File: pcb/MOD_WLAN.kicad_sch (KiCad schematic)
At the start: 21 parts, among them IC2 ESP32-C6-WROOM-1-N8, SW1 SW_DIP_x01

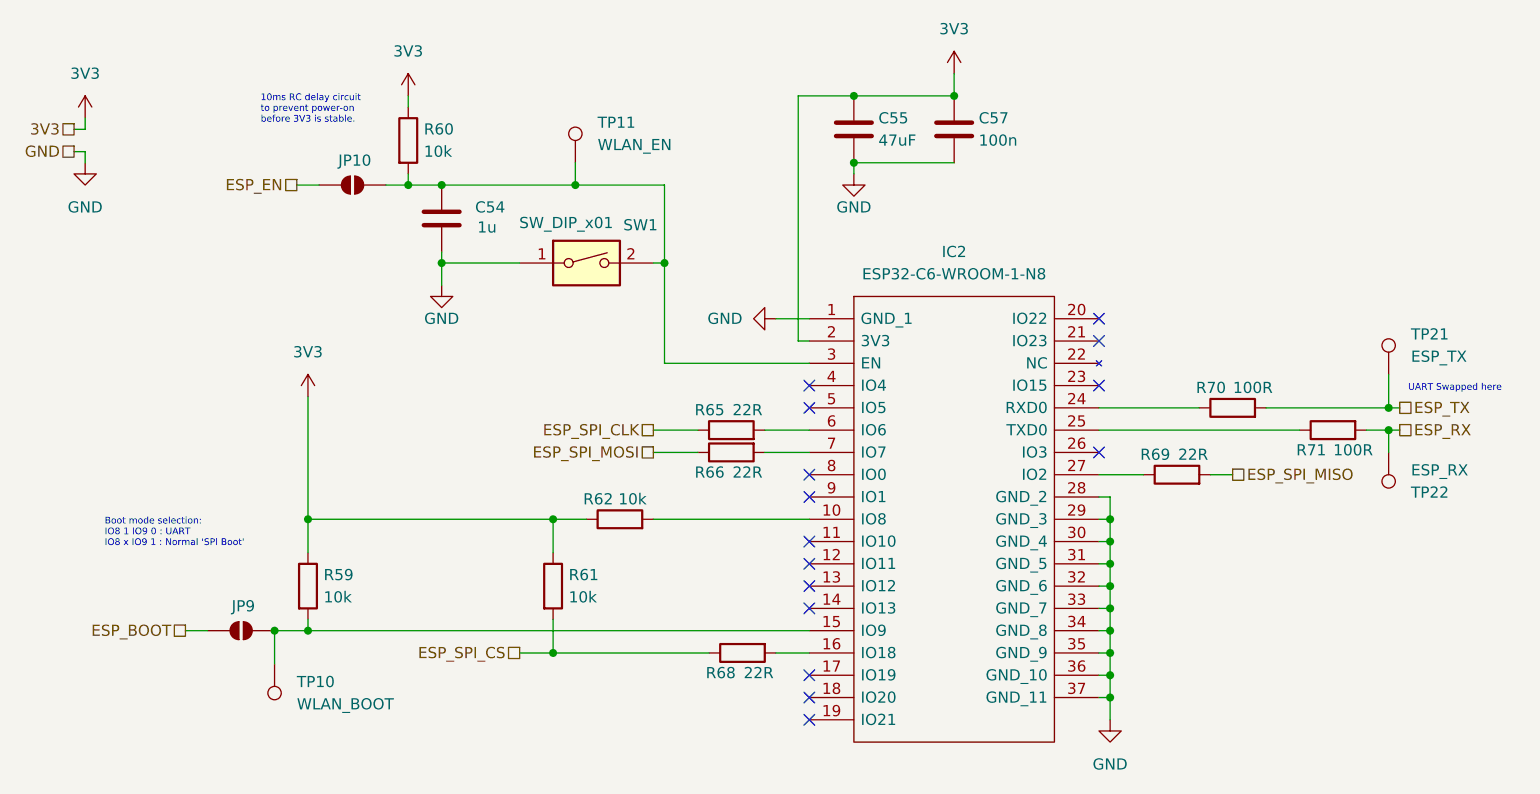
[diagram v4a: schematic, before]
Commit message: initial routing of power for pcie, swapped switches for jumpers
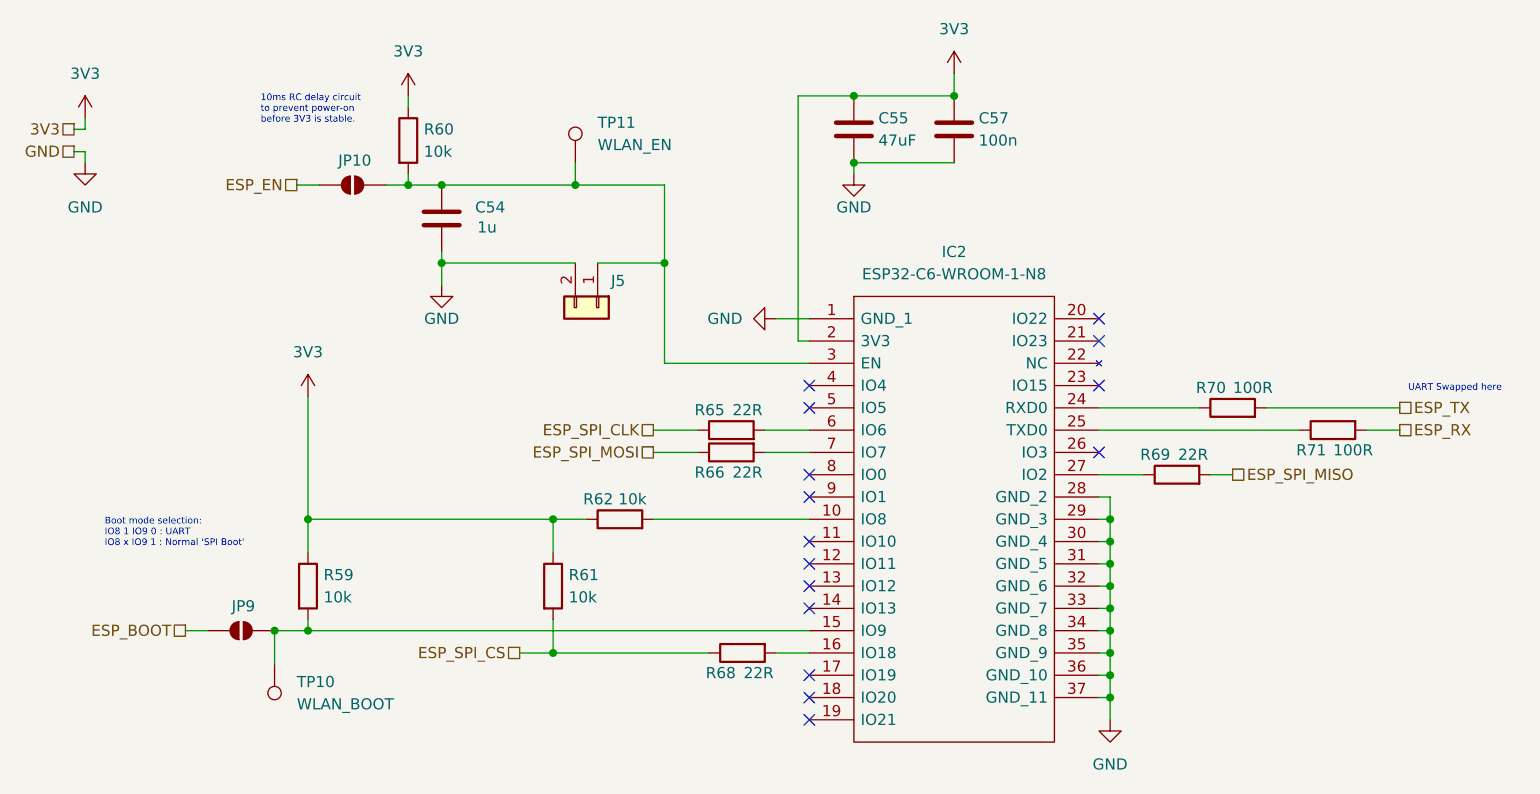
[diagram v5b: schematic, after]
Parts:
- removed SW1: SW_DIP_x01, SamacSys_Parts:EDS01SGNNTR04Q, symbol Switch:SW_DIP_x01
- removed TP21: ESP_TX, TestPoint:TestPoint_THTPad_D2.0mm_Drill1.0mm, symbol Connector:TestPoint
- removed TP22: ESP_RX, TestPoint:TestPoint_THTPad_D2.0mm_Drill1.0mm, symbol Connector:TestPoint
- added J5: Conn_01x02, Connector_PinHeader_2.54mm:PinHeader_1x02_P2.54mm_Vertical, symbol Connector_Generic:Conn_01x02
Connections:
- net GND: now also J5.2 (Pin_2)
- net at C54.1, IC2.3 (EN), JP10.2 (B)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: now also J5.1 (Pin_1)
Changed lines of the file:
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@@
-	)
-	(junction
-		(at 175.26 57.15)
-		(diameter 0)
-		(color 0 0 0 0)
 	)
 	(junction
@@
 	)
 	(junction
-		(at 175.26 59.69)
-		(diameter 0)
-		(color 0 0 0 0)
-	)
-	(junction
 		(at 143.51 87.63)
 		(diameter 0)
@@
 	(wire
 		(pts
-			(xy 67.31 40.64) (xy 76.2 40.64)
+			(xy 67.31 40.64) (xy 82.55 40.64)
 		)
 		(stroke
@@
 	(wire
 		(pts
-			(xy 92.71 40.64) (xy 91.44 40.64)
-		)
-		(stroke
-			(width 0)
-			(type default)
-		)
-	)
-	(wire
-		(pts
 			(xy 143.51 72.39) (xy 142.24 72.39)
 		)
@@
 	(wire
 		(pts
-			(xy 175.26 53.34) (xy 175.26 57.15)
-		)
-		(stroke
-			(width 0)
-			(type default)
-		)
-	)
-	(wire
-		(pts
 			(xy 63.5 21.59) (xy 63.5 22.86)
 		)
@@
 	(wire
 		(pts
-			(xy 172.72 59.69) (xy 175.26 59.69)
-		)
-		(stroke
-			(width 0)
-			(type default)
-		)
-	)
-	(wire
-		(pts
 			(xy 142.24 80.01) (xy 143.51 80.01)
 		)
@@
 	(wire
 		(pts
-			(xy 175.26 59.69) (xy 176.53 59.69)
+			(xy 172.72 59.69) (xy 176.53 59.69)
 		)
 		(stroke
@@
 	(wire
 		(pts
-			(xy 175.26 57.15) (xy 176.53 57.15)
+			(xy 161.29 57.15) (xy 176.53 57.15)
 		)
 		(stroke
@@
 	(wire
 		(pts
+			(xy 85.09 40.64) (xy 92.71 40.64)
+		)
+		(stroke
+			(width 0)
+			(type default)
+		)
+	)
+	(wire
+		(pts
 			(xy 80.01 81.28) (xy 80.01 85.09)
 		)
@@
 	(wire
 		(pts
-			(xy 161.29 57.15) (xy 175.26 57.15)
-		)
-		(stroke
-			(width 0)
-			(type default)
-		)
-	)
-	(wire
-		(pts
 			(xy 67.31 40.64) (xy 67.31 39.37)
 		)
@@
 		(pts
 			(xy 67.31 31.75) (xy 82.55 31.75)
-		)
-		(stroke
-			(width 0)
-			(type default)
-		)
-	)
-	(wire
-		(pts
-			(xy 175.26 59.69) (xy 175.26 62.23)
 		)
 		(stroke
@@
 	)
 	(symbol
-		(lib_id "Switch:SW_DIP_x01")
-		(at 83.82 40.64 0)
-		(unit 1)
-		(exclude_from_sim no)
-		(in_bom yes)
-		(on_board yes)
-		(dnp no)
-		(property "Reference" "SW1"
-			(at 91.948 36.322 0)
-			(effects
-				(font
-					(size 1.27 1.27)
-				)
-				(justify right)
-			)
-		)
-		(property "Value" "SW_DIP_x01"
-			(at 86.868 36.068 0)
-			(effects
-				(font
-					(size 1.27 1.27)
-				)
-				(justify right)
-			)
-		)
-		(property "Footprint" "SamacSys_Parts:EDS01SGNNTR04Q"
-			(at 83.82 40.64 0)
-			(effects
-				(font
-					(size 1.27 1.27)
-				)
-				(hide yes)
-			)
-		)
-		(property "Datasheet" "~"
-			(at 83.82 40.64 0)
-			(effects
-				(font
-					(size 1.27 1.27)
-				)
-				(hide yes)
-			)
-		)
-		(property "Description" "1x DIP Switch, Single Pole Single Throw (SPST) switch, small symbol"
-			(at 83.82 40.64 0)
-			(effects
-				(font
-					(size 1.27 1.27)
-				)
-				(hide yes)
-			)
-		)
-		(pin "2"
-		)
-		(pin "1"
-		)
-		(instances
-			(project "NCU"
-				(path "/3aee14c3-5480-4f7c-989e-3fef81779034/0cdbc80d-6682-4488-acea-b93c92a9f88d"
-					(reference "SW1")
-					(unit 1)
-				)
-			)
-		)
-	)
-	(symbol
 		(lib_id "Device:R")
 		(at 63.5 26.67 0)
@@
 	)
 	(symbol
-		(lib_id "Connector:TestPoint")
-		(at 175.26 62.23 0)
-		(mirror x)
-		(unit 1)
-		(exclude_from_sim no)
-		(in_bom yes)
-		(on_board yes)
-		(dnp no)
-		(property "Reference" "TP22"
-			(at 177.8 66.8021 0)
-			(effects
-				(font
-					(size 1.27 1.27)
-				)
-				(justify left)
-			)
-		)
-		(property "Value" "ESP_RX"
-			(at 177.8 64.2621 0)
-			(effects
-				(font
-					(size 1.27 1.27)
-				)
-				(justify left)
-			)
-		)
-		(property "Footprint" "TestPoint:TestPoint_THTPad_D2.0mm_Drill1.0mm"
-			(at 180.34 62.23 0)
-			(effects
-				(font
-					(size 1.27 1.27)
-				)
-				(hide yes)
-			)
-		)
-		(property "Datasheet" "~"
-			(at 180.34 62.23 0)
-			(effects
-				(font
-					(size 1.27 1.27)
-				)
-				(hide yes)
-			)
-		)
-		(property "Description" "test point"
-			(at 175.26 62.23 0)
-			(effects
-				(font
-					(size 1.27 1.27)
-				)
-				(hide yes)
-			)
-		)
-		(pin "1"
-		)
-		(instances
-			(project "NCU"
-				(path "/3aee14c3-5480-4f7c-989e-3fef81779034/0cdbc80d-6682-4488-acea-b93c92a9f88d"
-					(reference "TP22")
-					(unit 1)
-				)
-			)
-		)
-	)
-	(symbol
 		(lib_id "Device:R")
 		(at 80.01 77.47 0)
@@
 	)
 	(symbol
-		(lib_id "Connector:TestPoint")
-		(at 175.26 53.34 0)
-		(unit 1)
-		(exclude_from_sim no)
-		(in_bom yes)
-		(on_board yes)
-		(dnp no)
-		(fields_autoplaced yes)
-		(property "Reference" "TP21"
-			(at 177.8 48.7679 0)
-			(effects
-				(font
-					(size 1.27 1.27)
-				)
-				(justify left)
-			)
-		)
-		(property "Value" "ESP_TX"
-			(at 177.8 51.3079 0)
-			(effects
-				(font
-					(size 1.27 1.27)
-				)
-				(justify left)
-			)
-		)
-		(property "Footprint" "TestPoint:TestPoint_THTPad_D2.0mm_Drill1.0mm"
-			(at 180.34 53.34 0)
-			(effects
-				(font
-					(size 1.27 1.27)
-				)
-				(hide yes)
-			)
-		)
-		(property "Datasheet" "~"
-			(at 180.34 53.34 0)
-			(effects
-				(font
-					(size 1.27 1.27)
-				)
-				(hide yes)
-			)
-		)
-		(property "Description" "test point"
-			(at 175.26 53.34 0)
-			(effects
-				(font
-					(size 1.27 1.27)
-				)
-				(hide yes)
-			)
-		)
-		(pin "1"
-		)
-		(instances
-			(project "NCU"
-				(path "/3aee14c3-5480-4f7c-989e-3fef81779034/0cdbc80d-6682-4488-acea-b93c92a9f88d"
-					(reference "TP21")
-					(unit 1)
-				)
-			)
-		)
-	)
-	(symbol
 		(lib_id "Device:R")
 		(at 151.13 64.77 90)
@@
 					(unit 1)
 				)
+			)
+		)
+	)
+	(symbol
+		(lib_id "Connector_Generic:Conn_01x02")
+		(at 85.09 45.72 270)
+		(unit 1)
+		(exclude_from_sim no)
+		(in_bom yes)
+		(on_board yes)
+		(dnp no)
+		(property "Reference" "J5"
+			(at 86.614 42.672 90)
+			(effects
+				(font
+					(size 1.27 1.27)
+				)
+				(justify left)
+			)
+		)
+		(property "Value" "Conn_01x02"
+			(at 87.63 46.9899 90)
+			(effects
+				(font
+					(size 1.27 1.27)
+				)
+				(justify left)
+				(hide yes)
+			)
+		)
+		(property "Footprint" "Connector_PinHeader_2.54mm:PinHeader_1x02_P2.54mm_Vertical"
+			(at 85.09 45.72 0)
+			(effects
+				(font
+					(size 1.27 1.27)
+				)
+				(hide yes)
+			)
+		)
+		(property "Datasheet" "~"
+			(at 85.09 45.72 0)
+			(effects
+				(font
+					(size 1.27 1.27)
+				)
+				(hide yes)
+			)
+		)
+		(property "Description" "Generic connector, single row, 01x02, script generated (kicad-library-utils/schlib/autogen/connector/)"
+			(at 85.09 45.72 0)
+			(effects
+				(font
+					(size 1.27 1.27)
+				)
+				(hide yes)
+			)
+		)
+		(pin "1"
+		)
+		(pin "2"
+		)
+		(instances
+			(project ""
+				(path "/3aee14c3-5480-4f7c-989e-3fef81779034/0cdbc80d-6682-4488-acea-b93c92a9f88d"
+					(reference "J5")
+					(unit 1)
+				)

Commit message: updates from bom release
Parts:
- C55: value 47uF -> 47u
- R6: renamed from R68; value 22R -> 22
- R65, R66, R69: value 22R -> 22
- R70, R71: value 100R -> 100
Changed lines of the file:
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@@
 			)
 		)
-		(property "Value" "100R"
+		(property "Value" "100"
 			(at 162.052 54.864 90)
 			(effects
@@
 			)
 		)
-		(property "Value" "22R"
+		(property "Value" "22"
 			(at 103.886 64.516 90)
 			(effects
@@
 			)
 		)
-		(property "Value" "22R"
+		(property "Value" "22"
 			(at 103.886 57.404 90)
 			(effects
@@
 			)
 		)
-		(property "Value" "100R"
+		(property "Value" "100"
 			(at 173.482 61.976 90)
 			(effects
@@
 			)
 		)
-		(property "Value" "47uF"
+		(property "Value" "47u"
 			(at 117.094 26.67 0)
 			(effects
@@
 		(on_board yes)
 		(dnp no)
-		(property "Reference" "R68"
+		(property "Reference" "R6"
 			(at 100.838 87.376 90)
 			(effects
@@
 			)
 		)
-		(property "Value" "22R"
+		(property "Value" "22"
 			(at 105.156 87.376 90)
 			(effects
@@
 			(project "NCU"
 				(path "/3aee14c3-5480-4f7c-989e-3fef81779034/0cdbc80d-6682-4488-acea-b93c92a9f88d"
-					(reference "R68")
+					(reference "R6")
 					(unit 1)
 				)
@@
 			)
 		)
-		(property "Value" "22R"
+		(property "Value" "22"
 			(at 154.686 62.484 90)
 			(effects
